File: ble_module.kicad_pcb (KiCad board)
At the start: 4 copper layers, 60 x 98 mm, 181 parts, among them IC1 TPS25730DREFR, J1 Conn_01x06_Pin, J10 Conn_01x04_Pin, J11 Conn_01x06_Pin, J12 Conn_Coaxial, J13 Conn_02x02_Counter_Clockwise, J14 Conn_02x02_Counter_Clockwise, J15 Conn_01x16_Socket, J16 Conn_02x02_Counter_Clockwise, J2 Conn_02x05_Odd_Even, J3 USB_C_Receptacle_USB2.0_16P, J4 Conn_01x02_Pin, J6 Micro_SD_Card, J7 0532610271, J8 Conn_01x02_Pin, J9 Conn_01x06_Pin, SW1 PTS526 SK15 SMTR2 LFS, U1 STM32WB55RCVx, U10 DLF162500LT-5028A1, U11 TAS2505IRGER, U12 TMP1075NDRLR, U2 TVS1800DRV, U3 INA180A1, U4 MX25L12833FM2I, U5 CAT24C256, U6 LD39200PU33R, U7 TPS62933, U8 AP63300WU-7, U9 LDL112PV18R, Y1 ECS-320-8-33-RWY-TR, Y2 ECS-.327-9-12R-TR

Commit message: Layout draft complete
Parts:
- removed J4: Conn_01x02_Pin, Connector_PinHeader_2.54mm:PinHeader_1x02_P2.54mm_Vertical
- removed LS1: CMS-151135-078S, jka_library:CMS-151135-078S
- added C17: 100 nF, Capacitor_SMD:C_0603_1608Metric, F.Cu at (147.9, 91.1)
- added C77: 1 uF, Capacitor_SMD:C_0603_1608Metric, F.Cu at (148.7, 115.3)
- added C78: 100 nF, Capacitor_SMD:C_0603_1608Metric, B.Cu at (171.0, 96.5)
- added D11: LED, Diode_SMD:D_0603_1608Metric, F.Cu at (156.0, 117.3)
- added D12: LED, Diode_SMD:D_0603_1608Metric, F.Cu at (144.1, 92.6)
- added D13: LED, Diode_SMD:D_0603_1608Metric, F.Cu at (181.7, 108.4)
- added D14: LED, Diode_SMD:D_0603_1608Metric, F.Cu at (183.2, 108.4)
- added D15: ESD5Zxx, Diode_SMD:D_SOD-523, B.Cu at (184.5, 125.2)
- added D16: LED, Diode_SMD:D_0603_1608Metric, F.Cu at (147.9, 101.2)
- added J17: Conn_01x01_Pin, Connector_PinHeader_2.54mm:PinHeader_1x01_P2.54mm_Vertical, F.Cu at (155.2, 100.7)
- added J18: Conn_02x05_Odd_Even, Connector_PinHeader_1.27mm:PinHeader_2x05_P1.27mm_Vertical, F.Cu at (155.0, 91.7)
- added J19: Conn_01x02_Pin, Connector_PinHeader_2.54mm:PinHeader_1x02_P2.54mm_Vertical, F.Cu at (162.1, 131.7)
- added J20: Conn_01x04_Pin, Connector_PinHeader_2.54mm:PinHeader_1x04_P2.54mm_Vertical, F.Cu at (155.2, 105.5)
- added J21: Conn_01x02_Pin, Connector_PinHeader_2.54mm:PinHeader_1x02_P2.54mm_Vertical, F.Cu at (139.9, 96.5)
- added J5: Conn_01x02_Pin, Connector_PinHeader_2.54mm:PinHeader_1x02_P2.54mm_Vertical, F.Cu at (142.8, 75.5)
- added R22: 10k, Resistor_SMD:R_0603_1608Metric, B.Cu at (158.8, 99.7)
- added R23: 1k, Resistor_SMD:R_0603_1608Metric, B.Cu at (156.0, 117.3)
- added R52: R_US, Resistor_SMD:R_0603_1608Metric, B.Cu at (183.2, 108.4)
- added R53: R_US, Resistor_SMD:R_0603_1608Metric, B.Cu at (147.9, 101.2)
- added RN1: EXB-38VR000V, jka_library:EXB38V472JV, B.Cu at (159.1, 92.8)
- added RN2: EXB-38VR000V, jka_library:EXB38V472JV, B.Cu at (117.5, 78.3)
- added SW2: DS04-254-2-01BK-SMT, jka_library:DS04254201BKSMT, F.Cu at (149.7, 96.2)
- added SW3: TPS22919DCKR, jka_library:SOT65P210X110-6N, F.Cu at (146.1, 115.1)
- added TP1: TestPoint, TestPoint:TestPoint_Pad_D1.0mm, F.Cu at (112.2, 94.3)
- added TP2: TestPoint, TestPoint:TestPoint_Pad_D1.0mm, F.Cu at (114.1, 90.1)
- C18, C71: moved to F.Cu
- C23, C24, C40, C45, C47, C49, C51, C60, C62, C63, C64, C65, C66, C67, C68, C69, C70, J15, R1, R2, R24, R40, R45, R48: moved to B.Cu
- C54, C55: value 0.1 uF -> 1 uF
- D9: value LED -> ESD5Zxx; footprint Diode_SMD:D_0603_1608Metric -> Diode_SMD:D_SOD-523; moved to B.Cu
- J10: value Conn_01x04_Pin -> Conn_01x03_Pin; footprint Connector_PinHeader_2.54mm:PinHeader_1x04_P2.54mm_Vertical -> Connector_PinHeader_2.54mm:PinHeader_1x03_P2.54mm_Vertical
- J11: value Conn_01x06_Pin -> Conn_02x05_Odd_Even; footprint Connector_PinHeader_2.54mm:PinHeader_1x06_P2.54mm_Vertical -> Connector_PinHeader_2.54mm:PinHeader_2x05_P2.54mm_Vertical
- J16: value Conn_02x02_Counter_Clockwise -> Conn_02x02
- J2: value Conn_02x05_Odd_Even -> Conn_01x06_Pin; footprint Connector_PinHeader_1.27mm:PinHeader_2x05_P1.27mm_Vertical -> Connector_PinHeader_2.54mm:PinHeader_1x06_P2.54mm_Vertical
- J8: value Conn_01x02_Pin -> Conn_01x03_Pin; footprint Connector_PinHeader_2.54mm:PinHeader_1x02_P2.54mm_Vertical -> Connector_PinHeader_2.54mm:PinHeader_1x03_P2.54mm_Vertical
- J9: value Conn_01x06_Pin -> Conn_01x02_Pin; footprint Connector_PinHeader_2.54mm:PinHeader_2x03_P2.54mm_Vertical -> Connector_PinHeader_2.54mm:PinHeader_1x02_P2.54mm_Vertical
- R29: value R -> 0R; moved to B.Cu
- R41: value 0k -> 1k; moved to B.Cu
- R44: value 0R -> 1k
- R50: value 0R -> 22R; moved to B.Cu
- R51: value 0R -> R_US; moved to B.Cu
- moved U12 111.3 mm to (150.9, 132.4)
- moved C60 109.7 mm to (150.9, 132.4), turned to 180 degrees
- moved ANT1 108.9 mm to (201.6, 103.7), turned to 90 degrees
- moved H3 108.4 mm to (194.6, 131.2), turned to -90 degrees
- moved H1 107.3 mm to (194.6, 76.2), turned to -90 degrees
- moved R48 106.1 mm to (150.4, 127.8), turned to 0 degrees
- moved L7 102.1 mm to (196.8, 104.2), turned to 90 degrees
- moved C15 100.2 mm to (195.4, 103.7), turned to 0 degrees
- moved L6 98.2 mm to (194.0, 104.2), turned to 90 degrees
- moved C54 98.0 mm to (155.8, 127.9), turned to -90 degrees
- moved R40 97.8 mm to (153.4, 127.8), turned to 0 degrees
- moved C55 97.7 mm to (157.3, 127.9), turned to -90 degrees
- moved J15 95.7 mm to (187.1, 76.2), turned to 90 degrees
- moved C53 95.4 mm to (160.3, 126.1), turned to 0 degrees
- moved J7 95.3 mm to (168.5, 128.4), turned to 0 degrees
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- renumbered IC1 to U13
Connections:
- net /DC-DC Converter/BUCK_OUT renamed 3V6_BUCK_OUT
- net /OSC32_IN renamed /Controller/OSC32_IN
- net /OSC32_OUT renamed /Controller/OSC32_OUT
- net /OSC_IN renamed /Controller/OSC_IN
- net /OSC_OUT renamed /Controller/OSC_OUT
- net /Power/VBUS_RAW-1 renamed /Power/VBUS_RAW_1
- net /Power/VBUS_RAW-2 renamed /Power/VBUS_RAW_2
- net /RF1 renamed RF1
- net /STM_NRST renamed STM_NRST
- net /SWO renamed USART_RTS
- net /USB_D+ renamed USB_D+
- net /USB_D- renamed USB_D-
- net Net-(U8-SW) renamed /DC-DC Converter/5V_BUCK_SW
- B1 pad 1: /3V3_RTC -> unconnected-(B1-Pad1)
- B1 pad 3: /3V3_RTC -> 3V_RTC
- C10 pad 1: /VBUS_MAIN -> VBUS_MAIN
- C11 pad 1: /VBUS_MAIN -> VBUS_MAIN
- C18 pad 2: unconnected-(C18-Pad2) -> +3V3
- C25 pad 1: /VBUS_MAIN -> VBUS_MAIN
- C26 pad 2: GND -> Net-(C26-Pad2)
- C27 pad 1: /VBUS_MAIN -> VBUS_MAIN
- C29 pad 1: /VBUS_MAIN -> VBUS_MAIN
- C36 pad 1: /VBUS_MAIN -> VBUS_MAIN
- C54 pad 1: Net-(C54-Pad1) -> /Audio/AINL
- C55 pad 1: Net-(C55-Pad1) -> /Audio/AINR
- C57 pad 2: Net-(C57-Pad2) -> /Audio/SPK_OUT_M
- C59 pad 2: Net-(C57-Pad2) -> /Audio/SPK_OUT_M
- C7 pad 1: /VBUS_MAIN -> VBUS_MAIN
- D7 pad 1: /SPI1_MISO -> SPI2_MISO
- D7 pad 2: /SPI1_SCK -> SPI2_SCK
- D7 pad 4: /SPI1_MOSI -> SPI2_MOSI
- D7 pad 5: /SPI1_NSS -> SPI2_NSS
- D9 pad 1: /DC-DC Converter/BUCK_SS/PG -> /Serial Memory/DAT1
- D9 pad 2: Net-(D9-A) -> GND
- J1 pad 1: /RESET -> GND
- J1 pad 2: /VDD -> +3V3
- J1 pad 3: GND -> /Headers/JTMS_SWDIO_2
- J1 pad 4: /JTMS_SWDIO -> /Headers/JTCLK_SWCLK_2
- J1 pad 5: /JTCLK_SWCLK -> /Headers/SWO_2
- J1 pad 6: unconnected-(J1-Pin_6-Pad6) -> /Headers/STM_NRST_2
- J10 pad 1: /SPI1_NSS -> QSPI_IO2
- J10 pad 2: /SPI1_MOSI -> QSPI_IO1
- J10 pad 3: /SPI1_SCK -> QSPI_NCS
- J11 pad 2: /USART_CTS -> SPI2_NSS
- J11 pad 4: /USART_RX -> SPI2_NSS2
- J11 pad 5: /USART_TX -> GPIO1
- J11 pad 6: /USART_RTS -> SPI2_MOSI
- J15 pad 10: /LCD_DB3 -> LCD_DB3
- J15 pad 4: /LCD_REG_SEL -> LCD_REG_SEL
- J15 pad 5: /LCD_R/W -> LCD_R/W
- J15 pad 6: /LCD_EN -> LCD_EN
- J15 pad 7: /LCD_DB0 -> LCD_DB0
- J15 pad 8: /LCD_DB1 -> LCD_DB1
- J15 pad 9: /LCD_DB2 -> LCD_DB2
- J2 pad 1: +3V3 -> GND
- J2 pad 2: /JTMS_SWDIO -> USART_CTS
- J2 pad 3: GND -> +3V3
- J2 pad 4: /JTCLK_SWCLK -> USART_RX
- J2 pad 5: GND -> USART_TX
- J6 pad 2: /SPI1_NSS -> SPI2_NSS
- J6 pad 3: /SPI1_MOSI -> SPI2_MOSI
- J6 pad 5: /SPI1_SCK -> SPI2_SCK
- J6 pad 7: /SPI1_MISO -> SPI2_MISO
- J7 pad 1: Net-(J7-Pad1) -> /Audio/SPK_OUT_M
- J7 pad 2: Net-(J7-Pad2) -> /Audio/SPK_OUT_P
- J8 pad 1: /I2C_SDA -> QSPI_IO0
- J8 pad 2: /I2C_SCL -> QSPI_CLK_PIN
- J9 pad 1: /QSPI_CLK -> /Audio/AINR_IN
- J9 pad 2: /QSPI_IO1 -> /Audio/AINL_IN
- L5 pad 2: Net-(C57-Pad2) -> /Audio/SPK_OUT_M
- R1 pad 2: /I2C_SCL -> I2C_SCL
- R2 pad 2: /I2C_SDA -> I2C_SDA
- R24 pad 2: /QSPI_NCS -> QSPI_NCS
- R25 pad 1: /SPI1_MISO -> SPI2_MISO
- R26 pad 2: /SPI1_NSS -> SPI2_NSS
- R29 pad 1: Net-(D9-A) -> GND
- R29 pad 2: +3V3 -> Net-(C26-Pad2)
- R36 pad 1: /VBUS_MAIN -> GND
- R36 pad 2: /+5V_EN -> +5V_EN
- R37 pad 1: +5V -> GND
- R37 pad 2: /+1V8_EN -> +1V8_EN
- R40 pad 2: /~{AUDIO_RST} -> ~{AUDIO_RST}
- R41 pad 2: /Audio/IOVDD -> Net-(C26-Pad2)
- R44 pad 1: /Audio/AINL -> Net-(D12-K)
- R44 pad 2: Net-(C54-Pad1) -> GND
- R45 pad 1: /Audio/AINR -> SAI_SCK_B/SWO
- R45 pad 2: Net-(C55-Pad1) -> SWO
- R48 pad 1: /TEMP_ALERT -> TEMP_ALERT
- R50 pad 1: Net-(J7-Pad1) -> QSPI_CLK
- R50 pad 2: Net-(C57-Pad2) -> QSPI_CLK_PIN
- R51 pad 1: Net-(J7-Pad2) -> Net-(D13-K)
- R51 pad 2: /Audio/SPK_OUT_P -> GND
- U1 pad 1: /3V3_RTC -> 3V_RTC
- U1 pad 10: unconnected-(U1-PC1-Pad10) -> SPI2_MOSI
- U1 pad 11: unconnected-(U1-PC2-Pad11) -> SPI2_MISO
- U1 pad 12: /SAI_SD_A -> GPIO3
- U1 pad 15: unconnected-(U1-PA0-Pad15) -> GPIO2
- U1 pad 16: /SPI1_SCK -> ~{AUDIO_RST}
- U1 pad 17: /QSPI_NCS -> QSPI_NCS
- U1 pad 18: /QSPI_CLK -> QSPI_CLK
- U1 pad 19: /SPI1_NSS -> SAI_FS_B
- U1 pad 2: unconnected-(U1-PC13-Pad2) -> AUDIO_GPIO
- U1 pad 20: unconnected-(U1-PA5-Pad20) -> SAI_SD_B
- U1 pad 21: /QSPI_IO3 -> QSPI_IO3
- U1 pad 22: /QSPI_IO2 -> QSPI_IO2
- U1 pad 23: /MCLK_OUT -> GPIO1
- U1 pad 24: /USART_TX -> LED1
- U1 pad 25: unconnected-(U1-PC4-Pad25) -> LED2
- U1 pad 28: unconnected-(U1-PB10-Pad28) -> SPI2_SCK
- U1 pad 29: unconnected-(U1-PB11-Pad29) -> SPI2_NSS2
- U1 pad 38: /RX_TX_MOD_EXT_PA -> LCD_REG_SEL
- U1 pad 39: unconnected-(U1-PB1-Pad39) -> LCD_R/W
- U1 pad 40: unconnected-(U1-PE4-Pad40) -> LCD_EN
- U1 pad 42: unconnected-(U1-VSSSMPS-Pad42) -> GND
- U1 pad 44: unconnected-(U1-VDDSMPS-Pad44) -> +3V3
- U1 pad 46: /SAI_FS_A -> LCD_DB0
- U1 pad 47: /SAI_SCK_A -> I2C_SCL
- U1 pad 48: /SAI_MCLK_A -> I2C_SDA
- U1 pad 49: unconnected-(U1-PB15-Pad49) -> LCD_DB1
- U1 pad 5: /BOOT0 -> BOOT0
- U1 pad 50: unconnected-(U1-PC6-Pad50) -> LCD_DB2
- U1 pad 51: /USART_RX -> LCD_DB3
- U1 pad 54: /JTMS_SWDIO -> JTMS_SWDIO
- U1 pad 56: /JTCLK_SWCLK -> JTCLK_SWCLK
- U1 pad 57: unconnected-(U1-PA15-Pad57) -> RCC_MCC_OUT
- U1 pad 58: unconnected-(U1-PC10-Pad58) -> EEPROM_WP
- U1 pad 59: unconnected-(U1-PC11-Pad59) -> +5V_EN
- U1 pad 6: /QSPI_IO1 -> QSPI_IO1
- U1 pad 60: unconnected-(U1-PC12-Pad60) -> +1V8_EN
- U1 pad 61: unconnected-(U1-PD0-Pad61) -> SPI2_NSS
- U1 pad 62: unconnected-(U1-PD1-Pad62) -> TEMP_ALERT
- U1 pad 63: unconnected-(U1-PB3-Pad63) -> SAI_SCK_B/SWO
- U1 pad 64: /SPI1_MISO -> SAI_MCLK_B
- U1 pad 65: /SPI1_MOSI -> AUDIO_IOVDD_EN
- U1 pad 66: /I2C_SCL -> USART_TX
- U1 pad 67: /I2C_SDA -> USART_RX
- U1 pad 7: /QSPI_IO2 -> QSPI_IO0
- U1 pad 9: unconnected-(U1-PC0-Pad9) -> VBUS_SENSE
- U11 pad 13: /SAI_SD_A -> SAI_SD_B
- U11 pad 14: /SAI_SCK_A -> SAI_FS_B
- U11 pad 15: /SAI_FS_A -> SAI_SCK_B/SWO
- U11 pad 16: /SAI_MCLK_A -> SAI_MCLK_B
- U11 pad 17: /Audio/INTx -> AUDIO_GPIO
- U11 pad 18: /AUDIO_GPIO -> Net-(D11-A)
- U11 pad 19: /I2C_SCL -> I2C_SCL
- U11 pad 2: /~{AUDIO_RST} -> ~{AUDIO_RST}
- U11 pad 20: /I2C_SDA -> I2C_SDA
- U12 pad 1: /I2C_SDA -> I2C_SCL
- U12 pad 3: /TEMP_ALERT -> TEMP_ALERT
- U12 pad 6: /I2C_SCL -> I2C_SDA
- U13 pad 20: /VBUS_MAIN -> VBUS_MAIN
- U13 pad 21: /VBUS_MAIN -> VBUS_MAIN
- U13 pad 22: /VBUS_MAIN -> VBUS_MAIN
- U13 pad 41: /VBUS_MAIN -> VBUS_MAIN
- U13 pad 8: /I2C_SDA -> I2C_SDA
- U13 pad 9: /I2C_SCL -> I2C_SCL
- U3 pad 1: /VBUS_SENSE -> VBUS_SENSE
- U4 pad 1: /QSPI_NCS -> QSPI_NCS
- U4 pad 2: /QSPI_IO2 -> QSPI_IO1
- U4 pad 3: /QSPI_IO3 -> QSPI_IO2
- U4 pad 5: /QSPI_IO1 -> QSPI_IO0
- U4 pad 6: /QSPI_CLK -> QSPI_CLK_PIN
- U4 pad 7: /QSPI_IO4 -> QSPI_IO3
- U5 pad 5: /I2C_SDA -> I2C_SDA
- U5 pad 6: /I2C_SCL -> I2C_SCL
- U5 pad 7: /EEPROM_WP -> EEPROM_WP
- U7 pad 3: /VBUS_MAIN -> VBUS_MAIN
- U8 pad 2: /+5V_EN -> +5V_EN
- U8 pad 3: /VBUS_MAIN -> VBUS_MAIN
- U9 pad 1: /+1V8_EN -> +1V8_EN
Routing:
- net +3V3: track 126.9 -> 470.7 mm, vias 5 -> 35
- net GND: track 22.5 -> 241.7 mm, vias 8 -> 441
- net I2C_SCL: track 0.00 -> 128.2 mm, vias 0 -> 8
- net I2C_SDA: track 0.00 -> 125.9 mm, vias 0 -> 8
- net VBUS_SENSE: track 0.00 -> 107.6 mm, vias 0 -> 2
- net SPI2_NSS: track 0.00 -> 75.9 mm, vias 0 -> 3
- net /Headers/JTMS_SWDIO_2: track 0.00 -> 58.2 mm, vias 0 -> 1
- net ~{AUDIO_RST}: track 0.00 -> 57.4 mm, vias 0 -> 5
- net /Headers/JTCLK_SWCLK_2: track 0.00 -> 57.0 mm, vias 0 -> 1
- net /Headers/STM_NRST_2: track 0.00 -> 56.8 mm, vias 0 -> 1
- net /Headers/SWO_2: track 0.00 -> 56.6 mm, vias 0 -> 1
- net TEMP_ALERT: track 0.00 -> 55.3 mm, vias 0 -> 1
- net SAI_SD_B: track 0.00 -> 49.8 mm, vias 0 -> 3
- net USART_RX: track 0.00 -> 48.8 mm, vias 0 -> 2
- net +5V_EN: track 0.00 -> 47.5 mm, vias 0 -> 2
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- added copper zone on F.Cu, net +5V
- added copper zone on F.Cu, net /DC-DC Converter/5V_BUCK_SW
- added copper zone on F.Cu, net /DC-DC Converter/BUCK_SW
- added copper zone on B.Cu, net /Power/DRAIN
- added copper zone on B.Cu, net /Power/VBUS_RAW_1
- added copper zone on F.Cu, net /Power/VBUS_RAW_1
- added copper zone on F.Cu, net /Power/VBUS_RAW_2
- added copper zone on F.Cu, net 3V6_BUCK_OUT
- added copper zone on B.Cu, net GND
- added copper zone on F.Cu, net GND
- added copper zone on In1.Cu, net GND
- added copper zone on In2.Cu, net GND
- added copper zone on F.Cu, net VBUS_MAIN
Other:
- board size 60 x 98 mm -> 107.5 x 60 mm
- board text added: "*"
- board text added: "1"
- board text added: "1V8"
- board text added: "2"
- board text added: "3"
- board text added: "3V BAT"
- board text added: "3V3"
- board text added: "5V"
- board text added: "Antenna GND Keepout Region"
- board text added: "BOOT"
- board text added: "CHAR LCD"
- board text added: "CLK"
- board text added: "CS"
- board text added: "CTS"
- board text added: "Current"
- board text added: "D0"
- board text added: "D1"
- board text added: "D2"
- board text added: "D3"
- board text added: "EN"
- board text added: "GPIO"
- board text added: "IO0"
- board text added: "IO2"
- board text added: "IO3"
- board text added: "Jakka1"
- board text added: "MCC"
- board text added: "MCLK"
- board text added: "MISO"
- board text added: "MOSI"
- board text added: "Max V"
- board text added: "MicroSD"
- board text added: "Min V"
- board text added: "NRST"
- board text added: "NSS"
- board text added: "NSS2"
- board text added: "PD3.1"
- board text added: "RESET"
- board text added: "RTS"
- board text added: "RW"
- board text added: "RX"
- board text added: "Rev. 1"
- board text added: "S/N"
- board text added: "SCK"
- board text added: "SCL"
- board text added: "SD"
- board text added: "SDA"
- board text added: "SEL"
- board text added: "SPI"
- board text added: "SPK"
- board text added: "SWCLK"
- board text added: "SWD"
- board text added: "SWDIO"
- board text added: "SWO"
- board text added: "TX"
- board text added: "USB"
- board text added: "USB CON"
- board text added: "V0"
- board text added: "WS"
- board text added: "x"
- board text removed: "${REFERENCE}"

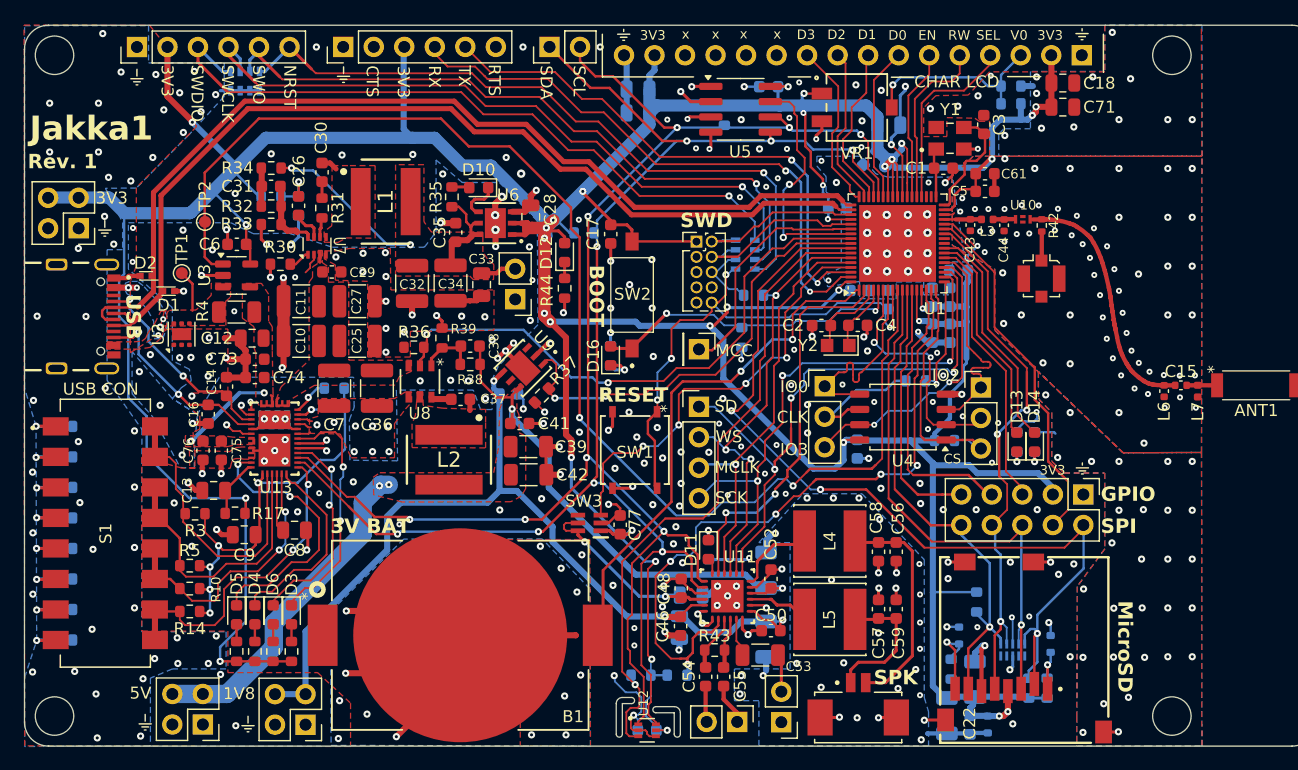
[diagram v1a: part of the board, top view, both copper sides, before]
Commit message: First draft of design output, schematic, and layout complete
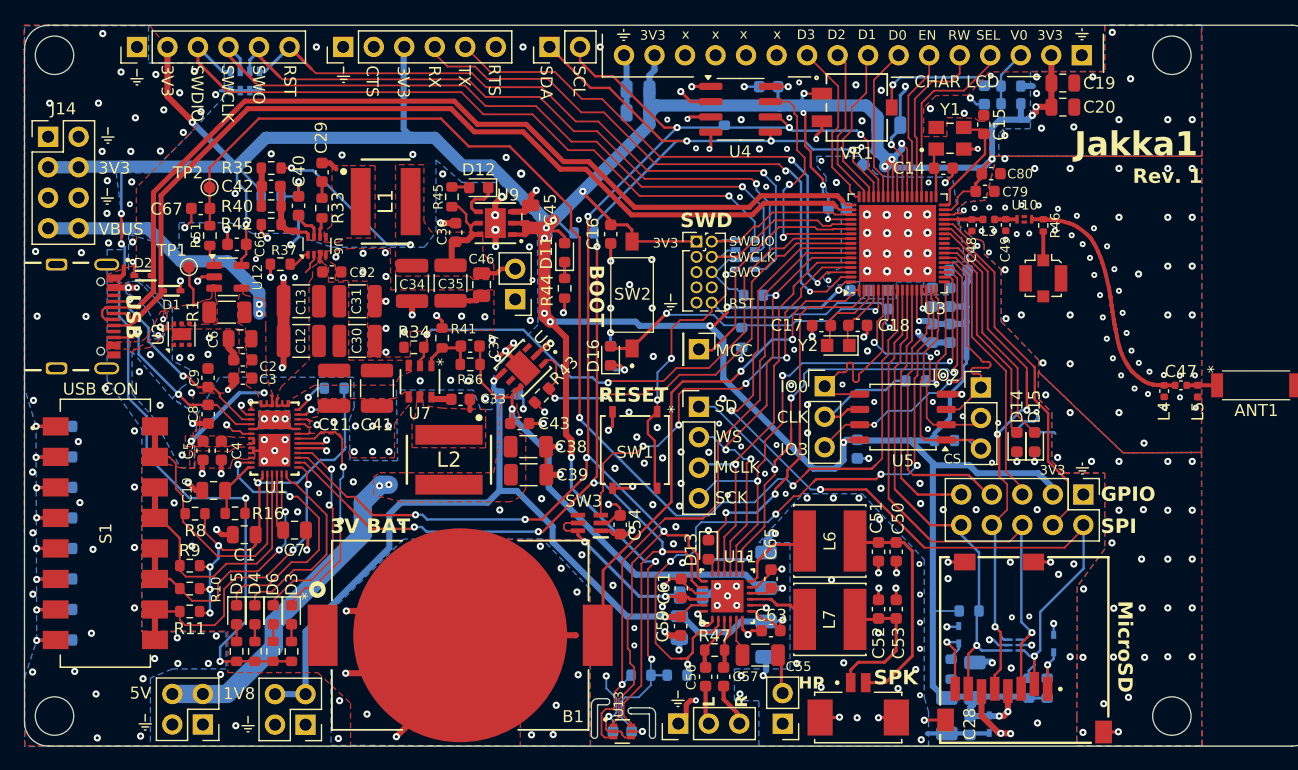
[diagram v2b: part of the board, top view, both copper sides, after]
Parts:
- removed the D15 at (184.5, 125.2)
- removed the J13 at (103.6, 90.6)
- added C21: 100 nF, Capacitor_SMD:C_0603_1608Metric, B.Cu at (179.0, 79.5)
- added C67: 100 nF, Capacitor_SMD:C_0603_1608Metric, F.Cu at (113.8, 89.0)
- added D10: PESD3V3X4UHMYL, jka_library:SON45P80X130X43-6N, B.Cu at (181.5, 125.3)
- added J14: Conn_02x04_Odd_Even, Connector_PinHeader_2.54mm:PinHeader_2x04_P2.54mm_Vertical, F.Cu at (101.1, 83.0)
- added R51: 1k, Resistor_SMD:R_0603_1608Metric, F.Cu at (114.5, 91.2)
- C17: renamed from C2; value 6 pF -> 12 pF
- C18: renamed from C4; value 6 pF -> 12 pF
- D1, D2: value ESD321DPYR -> ESD321x; footprint jka_library:DPY_R-PX1SON-N2_ -> jka_library:SODFL1608X77N
- D7: value PUSB3AB4Z -> ESD321x; footprint jka_library:SON50P100X250X50-10N -> jka_library:SODFL1608X77N
- D8, D9: value ESD5Zxx -> ESD321x; footprint Diode_SMD:D_SOD-523 -> jka_library:SODFL1608X77N
- J9: value Conn_01x02_Pin -> Conn_01x03_Pin; footprint Connector_PinHeader_2.54mm:PinHeader_1x02_P2.54mm_Vertical -> Connector_PinHeader_2.54mm:PinHeader_1x03_P2.54mm_Vertical
- R1: renamed from R4; value 0.025R -> 0.010R
- U12: renamed from U3; value INA180A1 -> INA180A3
- Y1: value ECS-320-8-33-RWY-TR -> ECS-320-8-33B2-CTN-TR3
- moved D8 8.68 mm to (184.8, 125.2), turned to 90 degrees
- moved D9 7.80 mm to (179.4, 131.9), turned to -90 degrees
- moved J9 4.90 mm to (153.5, 131.8), turned to 90 degrees
- moved D7 4.67 mm to (176.9, 124.4), turned to 90 degrees
- moved TP2 2.89 mm to (114.5, 87.2)
- moved C68 2.07 mm to (148.9, 132.5)
- moved U13 2.07 mm to (148.9, 132.5)
- moved C9 1.70 mm to (114.4, 103.0), turned to 90 degrees
- moved C2 1.01 mm to (117.3, 101.5)
- moved C3 1.01 mm to (117.3, 103.1)
- moved C6 1.01 mm to (117.0, 99.8)
- moved R31 0.97 mm to (177.7, 122.5), turned to 180 degrees
- moved R1 0.80 mm to (116.0, 97.6)
- moved TP1 0.77 mm to (112.8, 93.8)
- moved U12 0.73 mm to (116.0, 94.6)
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- renumbered C9 to C1, C13 to C10, C7 to C11, C10 to C12, C11 to C13, C1 to C14, C3 to C15, C17 to C16, C18 to C19, C73 to C2, C71 to C20, C72 to C22, C19 to C23, C23 to C25, C20 to C26, C21 to C27, C22 to C28, C30 to C29, C74 to C3, C25 to C30, C27 to C31, C29 to C32, C37 to C33, C32 to C34, C34 to C35, C35 to C36, C38 to C37, C39 to C38, C42 to C39, C75 to C4, C26 to C40, C36 to C41, C31 to C42, C41 to C43, C40 to C44, C28 to C45, C33 to C46, C15 to C47, C43 to C48, C44 to C49, C76 to C5, C56 to C50, C58 to C51, C57 to C52, C59 to C53, C77 to C54, C53 to C55, C54 to C56, C55 to C57, C45 to C58, C46 to C59, C12 to C6, C47 to C60, C48 to C61, C49 to C62, C50 to C63, C51 to C64, C52 to C65, C6 to C66, C60 to C68, C65 to C69, C8 to C7, C63 to C70, C64 to C71, C66 to C72, C68 to C73, C70 to C74, C67 to C75, C69 to C76, C62 to C77, C5 to C79, C16 to C8, C61 to C80, C14 to C9, D12 to D11, D10 to D12, D11 to D13, D13 to D14, D14 to D15, J3 to J1, J20 to J10, J1 to J11, J11 to J12, J18 to J13, J17 to J15, J2 to J16, J21 to J17, J8 to J18, J10 to J19, J15 to J2, J5 to J20, J6 to J3, J16 to J4, J14 to J5, J12 to J6, J19 to J8, L6 to L4, L7 to L5, L4 to L6, L5 to L7, R14 to R11, R6 to R12, R8 to R13, R11 to R14, R17 to R16, R7 to R17, R9 to R18, R12 to R19, R49 to R2, R16 to R20, R22 to R21, R1 to R22, R2 to R23, R45 to R24, R47 to R25, R46 to R26, R24 to R27, R50 to R28, R26 to R29, R13 to R3, R27 to R30, R25 to R31, R28 to R32, R31 to R33, R36 to R34, R34 to R35, R38 to R36, R30 to R37, R29 to R38, R41 to R39, R18 to R4, R32 to R40, R39 to R41, R33 to R42, R37 to R43, R35 to R45, R42 to R46, R43 to R47, R23 to R48, R40 to R49, R19 to R5, R48 to R50, R51 to R52, R52 to R53, R53 to R54, R20 to R6, R21 to R7, R3 to R8, R5 to R9, U13 to U1, U12 to U13, U1 to U3, U5 to U4, U4 to U5, U7 to U6, U8 to U7, U9 to U8, U6 to U9
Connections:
- net /Power/VBUS_RAW_1 renamed VBUS_FROM_CONN1
- net /Power/VBUS_RAW_2 renamed VBUS_FROM_CONN2
- C8 pad 1: GND -> /Power/USB_CC2
- C8 pad 2: /Power/USB_CC2 -> GND
- C9 pad 1: GND -> /Power/USB_CC1
- C9 pad 2: /Power/USB_CC1 -> GND
- D7 pad 1: SPI2_MISO -> /Serial Memory/DAT1
- D7 pad 2: SPI2_SCK -> GND
- D8 pad 1: +3V3 -> /Serial Memory/DAT2
- D9 pad 1: /Serial Memory/DAT1 -> +3V3
- J9 pad 1: /Audio/AINR_IN -> GND
- U12 pad 1: VBUS_SENSE -> Net-(R51-Pad1)
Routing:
- net VBUS_FROM_CONN2: track 8.52 -> 30.1 mm, vias 2 -> 4
- net VBUS_SENSE: track 107.6 -> 103.0 mm
- net +3V3: track 470.7 -> 474.0 mm, vias 35 -> 37
- net SPI2_NSS: track 75.9 -> 73.1 mm
- net Net-(R51-Pad1): track 0.00 -> 1.80 mm
- net SPI2_MISO: track 42.7 -> 41.5 mm
- net GND: track 241.7 -> 241.1 mm, vias 441 -> 446
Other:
- outline, holes or cut-outs redrawn
- board text added: "0.1270 mm / 0.1270 mm"
- board text added: "0.2000 mm"
- board text added: "1.6062 mm"
- board text added: "107.4996 mm x 60.0000 mm"
- board text added: "4"
- board text added: "BOARD CHARACTERISTICS"
- board text added: "Board Thickness:"
- board text added: "Board overall dimensions:"
- board text added: "Castellated pads:"
- board text added: "Copper Finish:"
- board text added: "Copper Layer Count:"
- board text added: "Edge card connectors:"
- board text added: "HP"
- board text added: "Impedance Control:"
- board text added: "L"
- board text added: "Min hole diameter:"
- board text added: "Min track/spacing:"
- board text added: "No"
- board text added: "None"
- board text added: "Plated Board Edge:"
- board text added: "R"
- board text added: "RST"
- board text added: "VBUS"
- board text added: "Yes"
- board text removed: "NRST"
